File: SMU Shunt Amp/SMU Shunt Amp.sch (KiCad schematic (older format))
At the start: 17 parts

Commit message: Schematic finished.
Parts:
- removed C?: 10u, symbol Device:C_Small
- removed C? (x2): 10u, symbol Device:CP1_Small
- added C1, C2, C4, C9: 10u, Capacitor_SMD:CP_Elec_6.3x7.7, symbol Device:CP1_Small
- added C10, C11, C7, C8: 100n, Capacitor_SMD:C_0805_2012Metric_Pad1.18x1.45mm_HandSolder, symbol Device:C_Small
- added C12, C13: Optional, Capacitor_SMD:C_0805_2012Metric_Pad1.18x1.45mm_HandSolder, symbol Device:C_Small
- added H1, H2, H3, H4: MountingHole, MountingHole:MountingHole_3.2mm_M3, symbol Mechanical:MountingHole
- added JP1: Signal Input, Connector_PinHeader_2.54mm:PinHeader_1x02_P2.54mm_Vertical, symbol Device:Jumper
- added JP2: 100uV Input, Connector_PinHeader_2.54mm:PinHeader_1x02_P2.54mm_Vertical, symbol Device:Jumper
- added JP3: Jumper, Connector_PinHeader_2.54mm:PinHeader_1x02_P2.54mm_Vertical, symbol Device:Jumper
- added JP4: Short to Ground, Connector_PinHeader_2.54mm:PinHeader_1x02_P2.54mm_Vertical, symbol Device:Jumper
- added R10: 0R, Resistor_SMD:R_0805_2012Metric_Pad1.20x1.40mm_HandSolder, symbol Device:R_US
- added R11, R12: 147R, Resistor_SMD:R_0805_2012Metric_Pad1.20x1.40mm_HandSolder, symbol Device:R_Small_US
- added R13: 15R, Resistor_SMD:R_0805_2012Metric_Pad1.20x1.40mm_HandSolder, symbol Device:R_Small_US
- added R4: 20K, Resistor_SMD:R_0805_2012Metric_Pad1.20x1.40mm_HandSolder, symbol Device:R_Small_US
- added R5: 1.65M, Resistor_SMD:R_0805_2012Metric_Pad1.20x1.40mm_HandSolder, symbol Device:R_Small_US
- added R6: 1M, Resistor_SMD:R_0805_2012Metric_Pad1.20x1.40mm_HandSolder, symbol Device:R_Small_US
- added R7: 11R, Resistor_SMD:R_0805_2012Metric_Pad1.20x1.40mm_HandSolder, symbol Device:R_Small_US
- added R8: 49.9R, Resistor_SMD:R_0805_2012Metric_Pad1.20x1.40mm_HandSolder, symbol Device:R_Small_US
- added R9: 49.9, Resistor_SMD:R_0805_2012Metric_Pad1.20x1.40mm_HandSolder, symbol Device:R_Small_US
- added TP1, TP2, TP3, TP4: TestPoint, TestPoint:TestPoint_Keystone_5010-5014_Multipurpose, symbol Connector:TestPoint
- C3, C6: renamed from C?; footprint (none) -> Capacitor_SMD:C_0805_2012Metric_Pad1.18x1.45mm_HandSolder
- C5: renamed from C?; value CP1_Small -> 10u; footprint (none) -> Capacitor_SMD:CP_Elec_6.3x7.7; PN (none) -> UCZ1J100MCS1GS
- D1: renamed from D?; footprint (none) -> Diode_SMD:D_SOD-128; PN (none) -> PMEG4050ETP,115
- J1: renamed from J?; value Screw_Terminal_01x02 -> 36VDV; footprint (none) -> TerminalBlock_Phoenix:TerminalBlock_Phoenix_PT-1,5-2-5.0-H_1x02_P5.00mm_Horizontal; PN (none) -> 1935161
- J2: renamed from J?; value Conn_Coaxial -> Input
- J3: renamed from J?; value Conn_Coaxial -> Output
- R1, R2, R3: renamed from R?; footprint (none) -> Resistor_SMD:R_0805_2012Metric_Pad1.20x1.40mm_HandSolder
- gave numbers to parts that had none: 4
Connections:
- net +15V: now also U3.5 (V+), U4.7 (V+), C1.1, C2.1, C7.1, C8.1, R4.1, R5.1, TP2.1
- net -15V: now also U3.2 (V-), U4.4 (V-), C10.2, C11.2, C2.2, C4.2, TP4.1
- net GND: now also J2.2 (Ext), J3.2 (Ext), C1.2, C10.1, C11.1, C4.1, C7.2, C8.2, C9.2, JP4.1, R12.2, R13.2, R7.2, R8.1, TP3.1
- net at U4.2 (-): now also C13.1, R10.2, R11.1, R12.1, R13.1
- net at U4.3 (+): now also U3.3 (+), JP1.2, JP2.2, JP4.2
- net at U4.6: now also C13.2, R11.2, R9.2
- net NULL: now reaches U4.8 (NULL)
- net NULL: now also R4.2, R6.1
- net at U3.1: now also C12.1, R6.2
- net at U3.4 (-): now also C12.2, R10.1
- net at J2.1 (In): now also JP1.1, JP3.2
- net at J3.1 (In): now also R9.1
- new net: C9.1, JP2.1, R5.2, R7.1, TP1.1
- new net: JP3.1, R8.2
- no-connect marks 0 -> 1
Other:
- moved on the sheet: C3, C5, C6, D1, J1, J2, J3, R1, R2, R3, U1, U2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

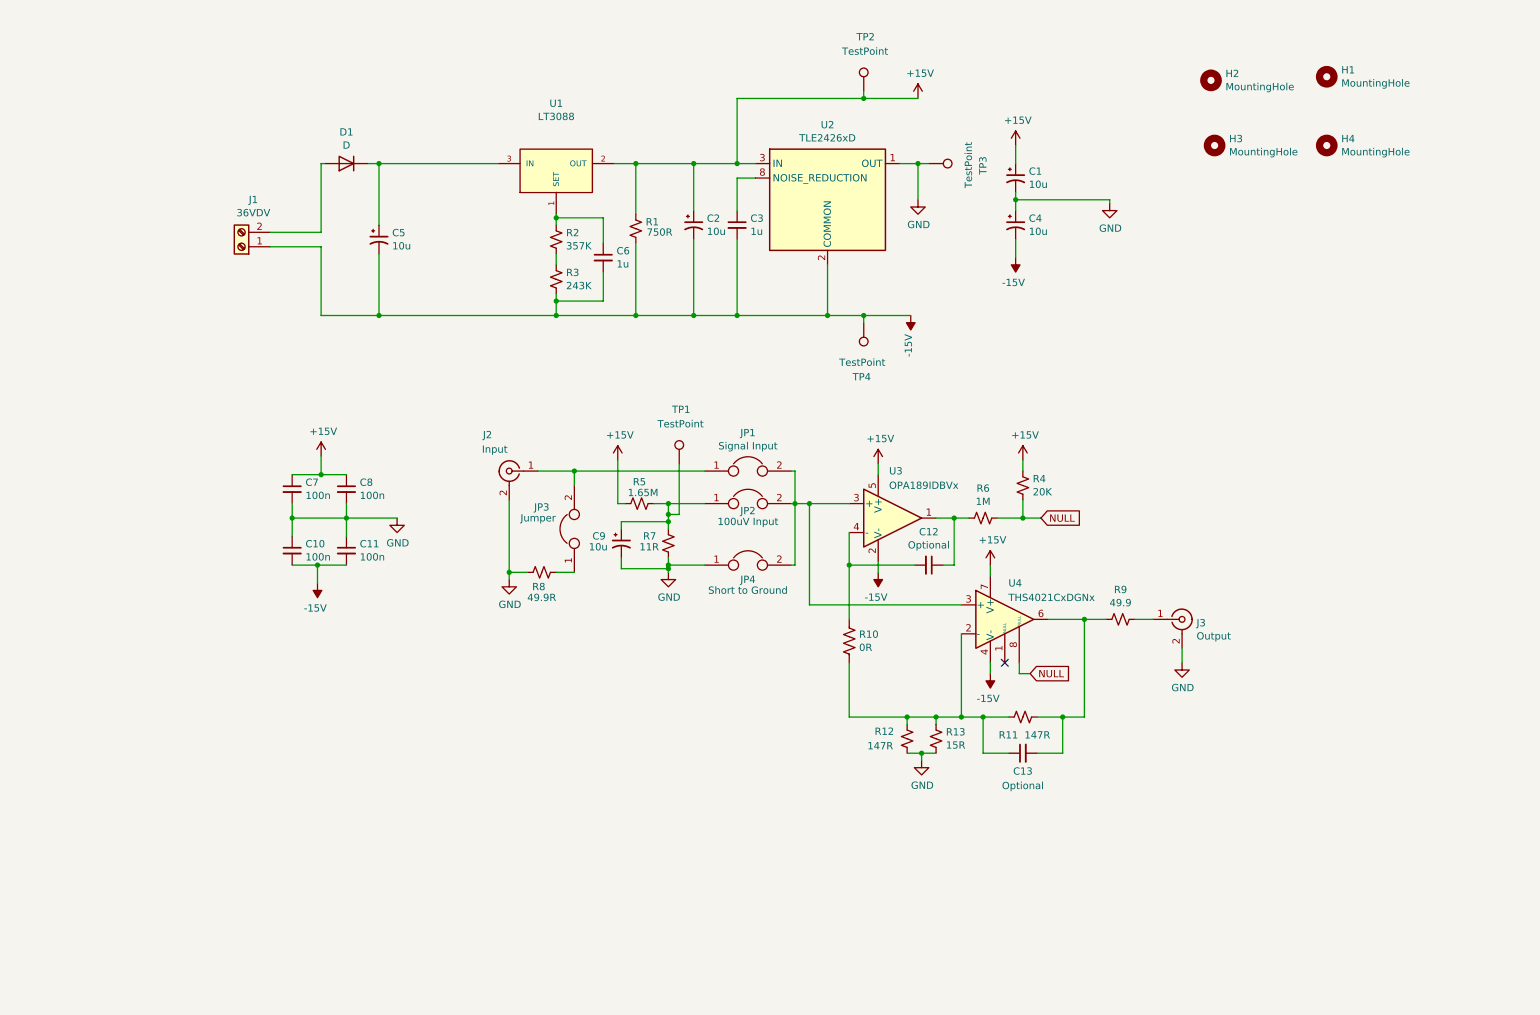
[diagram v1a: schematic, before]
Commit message: Reduce voltage rails to +/-14V
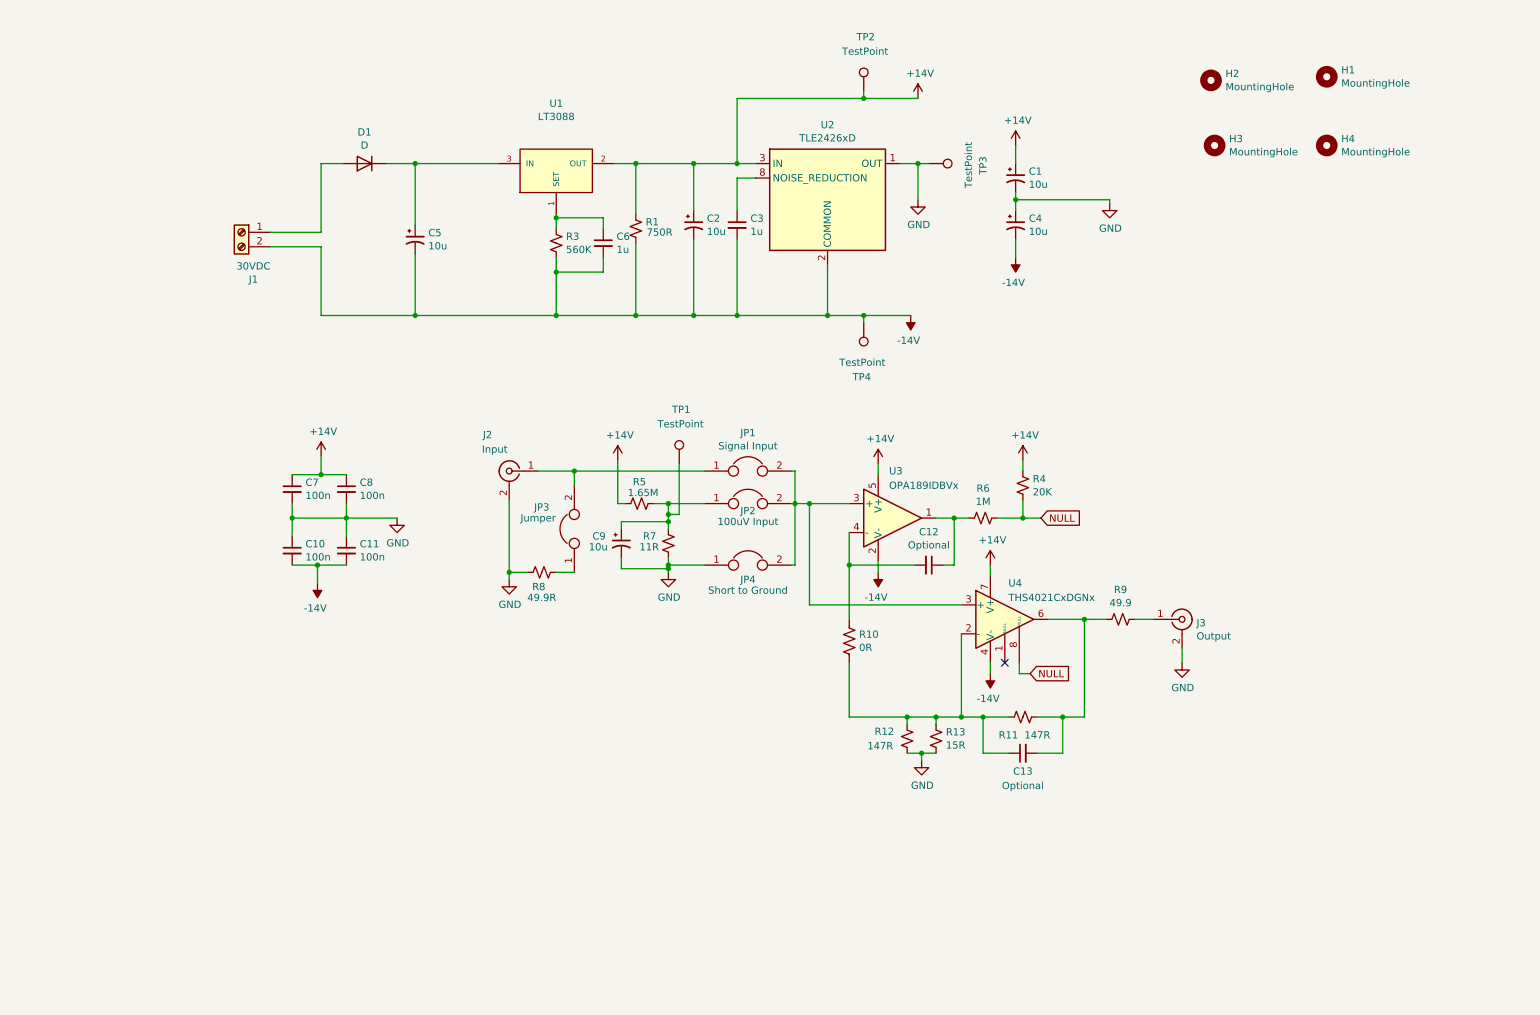
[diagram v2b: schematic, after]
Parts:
- removed R2: 357K, Resistor_SMD:R_0805_2012Metric_Pad1.20x1.40mm_HandSolder, symbol Device:R_Small_US
- J1: value 36VDV -> 30VDC
- R3: value 243K -> 560K
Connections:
- net -15V: now also J1.2 (Pin_2); no longer J1.1 (Pin_1)
- net at D1.2 (A): now also J1.1 (Pin_1); no longer J1.2 (Pin_2)
- net at C6.1, U1.1 (SET): now also R3.1
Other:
- moved on the sheet: C5, C6, D1, R3

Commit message: 90% finished routing PCB.
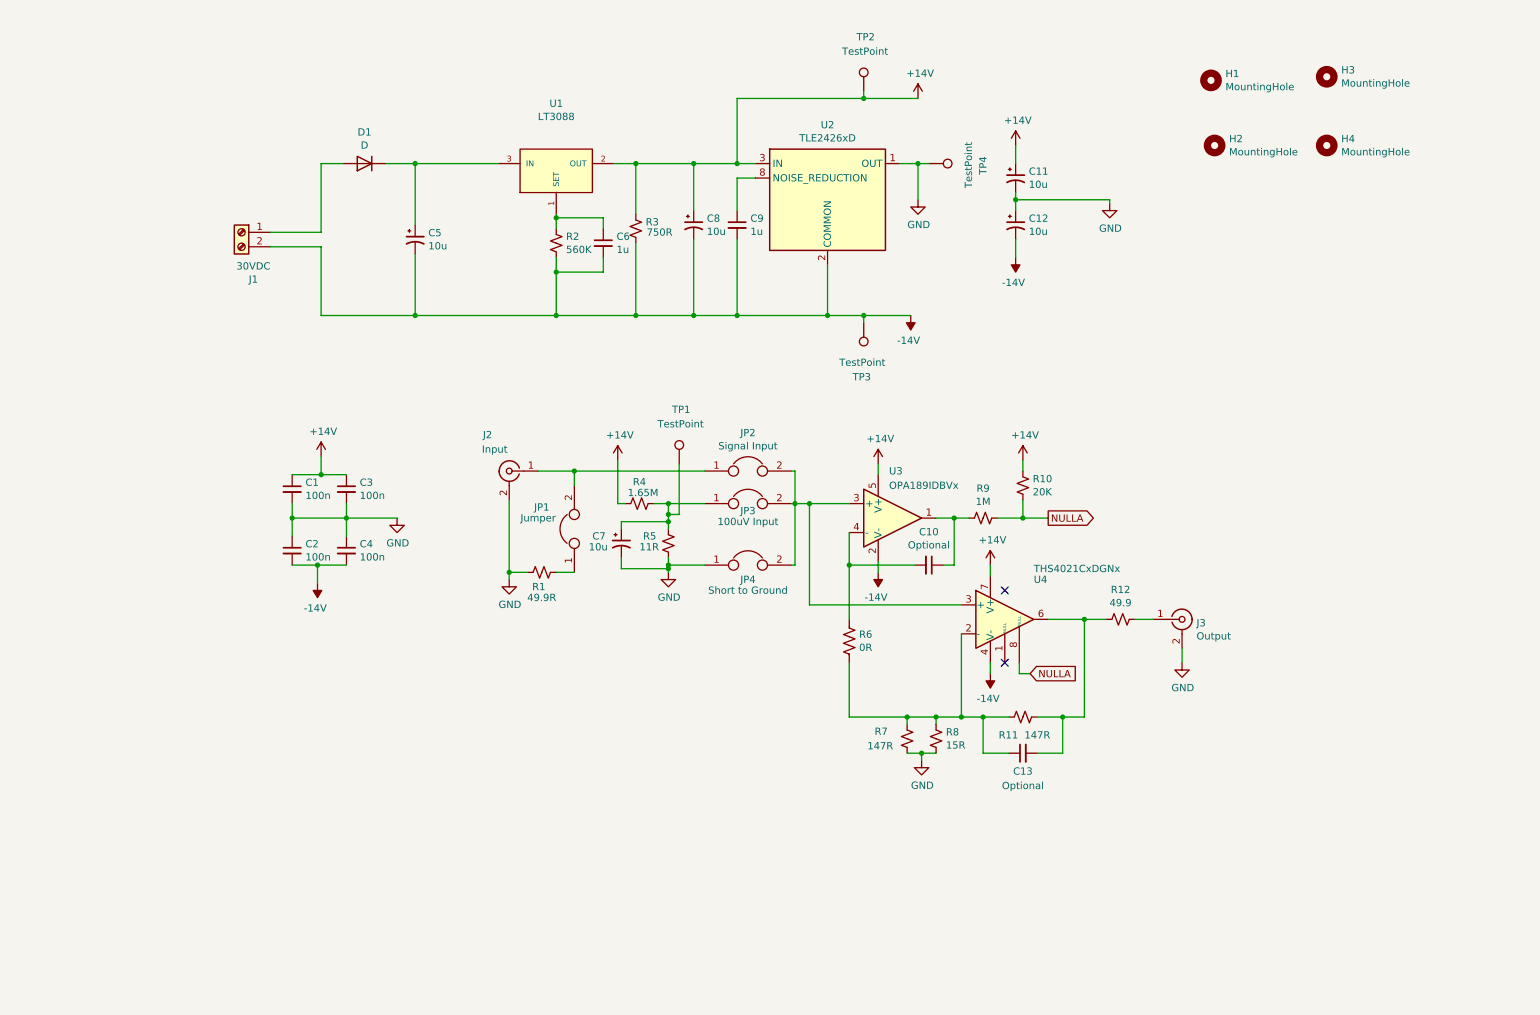
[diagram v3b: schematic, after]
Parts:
- renumbered C7 to C1, C12 to C10, C1 to C11, C4 to C12, C10 to C2, C8 to C3, C11 to C4, C9 to C7, C2 to C8, C3 to C9, H2 to H1, H3 to H2, H1 to H3, JP3 to JP1, JP1 to JP2, JP2 to JP3, R8 to R1, R4 to R10, R9 to R12, R3 to R2, R1 to R3, R5 to R4, R7 to R5, R10 to R6, R12 to R7, R13 to R8, R6 to R9, TP4 to TP3, TP3 to TP4
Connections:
- net NULL is gone; now on net NULLA: R10.2, R9.1, U4.8 (NULL)
- net NULLA: now reaches U4.8 (NULL)
- no-connect marks 1 -> 2

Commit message: Add part numbers to schematic.
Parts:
- added C5, C6: 100n, Capacitor_SMD:C_0805_2012Metric_Pad1.18x1.45mm_HandSolder, symbol Device:C_Small
- added R13, R9: 0R, Resistor_SMD:R_0805_2012Metric_Pad1.20x1.40mm_HandSolder, symbol Device:R_Small_US
- added U5: OPA1611AIDR, Package_SO:SOIC-8_3.9x4.9mm_P1.27mm, symbol MAGI_Symbols:OPA1611AIDR
- C1, C2, C3, C4: Part (none) -> C0805C103K5GEC7210
- C10: renamed from C8; PN UCZ1J100MCS1GS -> (none); Part (none) -> UCZ1J100MCS1GS
- C11: renamed from C9; Part (none) -> 08055C105K4T4A
- C13: Part (none) -> VJ0805A680GXAPW1BC
- C14: renamed from C11; PN UCZ1J100MCS1GS -> (none); Part (none) -> UCZ1J100MCS1GS
- C15: renamed from C12; PN UCZ1J100MCS1GS -> (none); Part (none) -> UCZ1J100MCS1GS
- C7: renamed from C5; PN UCZ1J100MCS1GS -> (none); Part (none) -> UCZ1J100MCS1GS
- C9: renamed from C6; Part (none) -> 08055C105K4T4A
- D1: PN PMEG4050ETP,115 -> (none); Part (none) -> PMEG4050ETP,115
- J2: PN 1-1337445-0 -> (none); Part (none) -> 1-1337445-0
- J3: Part (none) -> 1-1337445-0; pn 1-1337445-0 -> (none)
- JP1: value Jumper -> Term; Part (none) -> 22-28-5027
- JP2: value Signal Input -> SIG; Part (none) -> 22-28-5027
- JP3: value 100uV Input -> 100uV; Part (none) -> 22-28-5027
- JP4: value Short to Ground -> GND; Part (none) -> 22-28-5027
- R1: Part (none) -> CRCW080549R9FKEA
- R10: renamed from R9; Part (none) -> CRCW08051M00FKEA
- R11: renamed from R10; Part (none) -> CRCW080520K0FKEAC
- R12: renamed from R11; value 147R -> 1.47K; Distributor (none) -> Ampacity Systems; Part (none) -> RN73C2A1K47BTDF
- R14: renamed from R12; Part (none) -> CRCW080549R9FKEA
- R2: renamed from R4; Part (none) -> RC0805FR-071M65L
- R3: renamed from R5; Part (none) -> RQ73C2A11RBTDF
- R4: renamed from R2; Part (none) -> CRCW0805560KFKEA
- R5: renamed from R3; Part (none) -> CRCW0805750RFKEA
- R6: Part (none) -> CRCW08050000Z0EB
- R7: value 147R -> 1.47K; Distributor (none) -> Ampacity Systems; Part (none) -> RN73C2A1K47BTDF
- R8: Part (none) -> CPF0805B15RE1
- TP1: value TestPoint -> 100uV
- TP2: value TestPoint -> +14V
- TP3: value TestPoint -> -14V
- TP4: value TestPoint -> GND
- U1: Part (none) -> LT3088EST#PBF
- U2: renamed from U3; Part (none) -> OPA189IDBVR
- U3: renamed from U4; Part (none) -> THS4021IDGNR
- U4: renamed from U2; Part (none) -> TLE2426CDR
- renumbered C10 to C12, C7 to C8
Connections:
- wire segments 136 -> 153
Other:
- moved on the sheet: C1, C10, C11, C12, C13, C2, C3, C4, C8, J2, J3, JP1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

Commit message: Rev B changes. THS4021 footprint fix, nulling circuit corrections, gnd tp cur limit.
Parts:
- added R15: 1K, Resistor_SMD:R_0805_2012Metric_Pad1.20x1.40mm_HandSolder, symbol Device:R_Small_US
- J1: PN 1935161 -> 1729018
- R11: value 20K -> 56K
- R2: value 1.65M -> 1.54M
- U3: footprint Package_SO:TI_SO-PowerPAD-8_ThermalVias -> Package_SO:MSOP-8-1EP_3x3mm_P0.65mm_EP1.73x1.85mm_ThermalVias
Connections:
- wire segments 153 -> 152
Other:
- moved on the sheet: C1, C10, C11, C12, C13, C14, C15, C2, C3, C4, C5, C6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

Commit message: New composite staged CFB design.
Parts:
- removed C10, C7, C8: 10u, Capacitor_SMD:CP_Elec_6.3x7.7, symbol Device:CP1_Small
- removed C11: 1u, Capacitor_SMD:C_0805_2012Metric_Pad1.18x1.45mm_HandSolder, symbol Device:C_Small
- removed C13: Optional, Capacitor_SMD:C_0805_2012Metric_Pad1.18x1.45mm_HandSolder, symbol Device:C_Small
- removed C5, C6: 100n, Capacitor_SMD:C_0805_2012Metric_Pad1.18x1.45mm_HandSolder, symbol Device:C_Small
- removed D1: D, Diode_SMD:D_SOD-128, symbol Device:D
- removed J1: 30VDC, TerminalBlock_Phoenix:TerminalBlock_Phoenix_PT-1,5-2-5.0-H_1x02_P5.00mm_Horizontal, symbol Connector:Screw_Terminal_01x02
- removed JP1: Term, Connector_PinHeader_2.54mm:PinHeader_1x02_P2.54mm_Vertical, symbol Device:Jumper
- removed JP2: SIG, Connector_PinHeader_2.54mm:PinHeader_1x02_P2.54mm_Vertical, symbol Device:Jumper
- removed JP3: 100uV, Connector_PinHeader_2.54mm:PinHeader_1x02_P2.54mm_Vertical, symbol Device:Jumper
- removed JP4: GND, Connector_PinHeader_2.54mm:PinHeader_1x02_P2.54mm_Vertical, symbol Device:Jumper
- removed R10: 1M, Resistor_SMD:R_0805_2012Metric_Pad1.20x1.40mm_HandSolder, symbol Device:R_Small_US
- removed R11: 56K, Resistor_SMD:R_0805_2012Metric_Pad1.20x1.40mm_HandSolder, symbol Device:R_Small_US
- removed R12: 1.47K, Resistor_SMD:R_0805_2012Metric_Pad1.20x1.40mm_HandSolder, symbol Device:R_Small_US
- removed R13, R9: 0R, Resistor_SMD:R_0805_2012Metric_Pad1.20x1.40mm_HandSolder, symbol Device:R_Small_US
- removed R15: 1K, Resistor_SMD:R_0805_2012Metric_Pad1.20x1.40mm_HandSolder, symbol Device:R_Small_US
- removed R6: 0R, Resistor_SMD:R_0805_2012Metric_Pad1.20x1.40mm_HandSolder, symbol Device:R_US
- removed TP1: 100uV, TestPoint:TestPoint_Keystone_5010-5014_Multipurpose, symbol Connector:TestPoint
- removed TP2: +14V, TestPoint:TestPoint_Keystone_5010-5014_Multipurpose, symbol Connector:TestPoint
- removed TP3: -14V, TestPoint:TestPoint_Keystone_5010-5014_Multipurpose, symbol Connector:TestPoint
- removed TP4: GND, TestPoint:TestPoint_Keystone_5010-5014_Multipurpose, symbol Connector:TestPoint
- removed U1: LT3088, Package_TO_SOT_SMD:SOT-223, symbol MAGI_Symbols:LT3088
- removed U3: THS4021CxDGNx, Package_SO:MSOP-8-1EP_3x3mm_P0.65mm_EP1.73x1.85mm_ThermalVias, symbol MAGI_Symbols:THS4021CxDGNx
- removed U4: TLE2426xD, Package_SO:SOIC-8_3.9x4.9mm_P1.27mm, symbol Reference_Voltage:TLE2426xD
- removed U5: OPA1611AIDR, Package_SO:SOIC-8_3.9x4.9mm_P1.27mm, symbol MAGI_Symbols:OPA1611AIDR
- added C7: 715p, Capacitor_SMD:C_0805_2012Metric_Pad1.18x1.45mm_HandSolder, symbol Device:C_Small
- added D1, D2: MBRA340, Diode_SMD:D_SMA_Handsoldering, symbol Device:D_Schottky
- added D3: Vz=30, Diode_SMD:D_SOD-123, symbol Device:D_Zener_Small
- added J1: 30VDC, TerminalBlock_Phoenix:TerminalBlock_Phoenix_PT-1,5-3-5.0-H_1x03_P5.00mm_Horizontal, symbol Connector:Screw_Terminal_01x03
- added R6: 4.3K, Resistor_SMD:R_0805_2012Metric_Pad1.20x1.40mm_HandSolder, symbol Device:R_Small_US
- added U2: THS3092D, Package_SO:SOIC-8_3.9x4.9mm_P1.27mm, symbol MAGI_Symbols:THS3092D
- C9: value 1u -> 6.8p; Part 08055C105K4T4A -> (none)
- R2: value 1.54M -> 150R; Part RC0805FR-071M65L -> (none)
- R3: value 11R -> 14.7K; Part RQ73C2A11RBTDF -> (none)
- R4: value 560K -> 430R; Part CRCW0805560KFKEA -> (none)
- R5: value 750R -> 14.7K; Part CRCW0805750RFKEA -> (none)
- R7: value 1.47K -> 60.4R; Distributor Ampacity Systems -> (none); Part RN73C2A1K47BTDF -> (none)
- R8: value 15R -> 604R; Part CPF0805B15RE1 -> (none)
- renumbered C14 to C5, C15 to C6, C12 to C8, R14 to R9, U2 to U1
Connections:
- net labels removed: NULLA
- wire segments 152 -> 103
- no-connect marks 2 -> 0
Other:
- moved on the sheet: C1, C2, C3, C4, C5, C6, C8, J2, J3, R1, R9, U1

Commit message: PCB layout initial.
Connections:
- net at J1.1 (Pin_1): now also D2.1 (K); no longer D1.2 (A)
- net at J1.3 (Pin_3): now also D1.2 (A); no longer D2.1 (K)
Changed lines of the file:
@@
 F 4 "1729018" H 1325 1800 50  0001 C CNN "PN"
 	1    1325 1800
-	-1   0    0    -1
+	-1   0    0    1
 $EndComp
 $Comp
